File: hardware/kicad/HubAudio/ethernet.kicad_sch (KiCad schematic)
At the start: 29 parts, among them J1 RJ45_Abracon_ARJP11A-MASA-B-A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, U19 LAN8720A, U20 CDCLVC1102PW, X1 ASE-50.000MHZ-LC-T

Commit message: Finalize I2C and SPI control architecture
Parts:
- removed C55: 100nF, Capacitor_SMD:C_0805_2012Metric, symbol Device:C
- removed C56: 1uF, Capacitor_SMD:C_0805_2012Metric, symbol Device:C
- removed C57: 10uF, Capacitor_SMD:C_1206_3216Metric, symbol Device:C
- removed FB2: BLM18BB600SN1, Inductor_SMD:L_0603_1608Metric, symbol Device:FerriteBead
- removed R31, R32: 10K, Resistor_SMD:R_0805_2012Metric, symbol Device:R
- removed RN1: CAY16-49R9F4LF, Resistor_SMD:R_Array_Convex_4x0603, symbol Device:R_Network04_Split
- removed U20: CDCLVC1102PW, Package_SO:TSSOP-8_4.4x3mm_P0.65mm, symbol MIKILAB_CDCLVC1102PW:CDCLVC1102PW
- added R25, R77, R78, R79: 49.9, Resistor_SMD:R_0805_2012Metric, symbol Device:R
- added R80, R81: 33, Resistor_SMD:R_0805_2012Metric, symbol Device:R
- C47, C48, C49, C59, C60, C61: PNM (none) -> GRM21BR71H104KA01L
- C58: PNM (none) -> GRM31CR71E106KA12L
- C62: PNM (none) -> GRM2165C1H471JA01D
- C63: PNM (none) -> GCM21BR71E105KA56L
- R2, R30: value RC0603FR-07330RL -> 330; footprint Inductor_SMD:L_0603_1608Metric -> Resistor_SMD:R_0805_2012Metric; PNM (none) -> RC0805FR-07330RL
- R34: PNM (none) -> FRC0805F1212TS
- R35: PNM (none) -> RC0805FR-074K7L
- R37, R38, R39, R40: PNM (none) -> RC0805FR-0710KL
- U19: PNM (none) -> LAN8720A
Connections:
- net 3V3_ETHERNET: now also R35.1; no longer R35.2
- net ETH_50MHZ_CLOCK: now also R81.2
- net ETH_MDIO: now also R35.2; no longer R35.1
- net ETH_RXD0: now also R37.1
- net ETH_RXD1: now also R38.1
- net ETH_TXD0: no longer R37.1
- net ETH_TXD1: no longer R38.1
- net GND: no longer J1.10 (V-), J1.9 (V+)
- net at U19.20 (TXN): now also R78.1
- net at U19.21 (TXP): now also R77.1
- net at U19.22 (RXN): now also R25.1
- net at U19.23 (RXP): now also R79.1
- net at U19.5 (XTAL1/CLKIN): now also R80.2
- net at J1.1 (TD+): now also R77.2
- net at J1.2 (TD-): now also R78.2
- net at J1.3 (RD+): now also R79.2
- net at J1.6 (RD-): now also R25.2
- net at X1.3 (OUT): now also R80.1, R81.1
- no-connect marks 0 -> 3
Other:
- moved on the sheet: C49, R35, X1

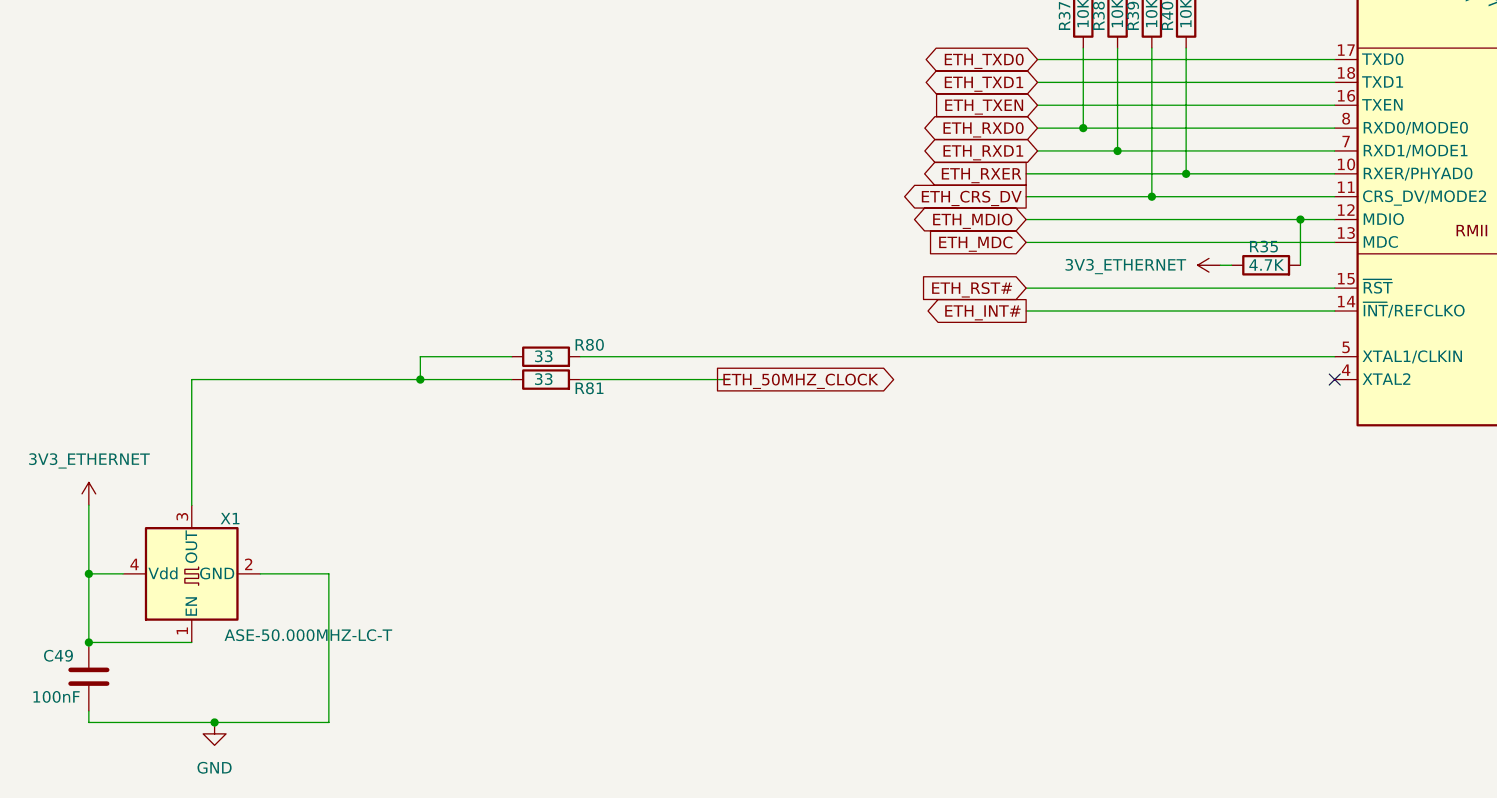
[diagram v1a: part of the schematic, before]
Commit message: Finalize HubAudio hardware architecture and PCB
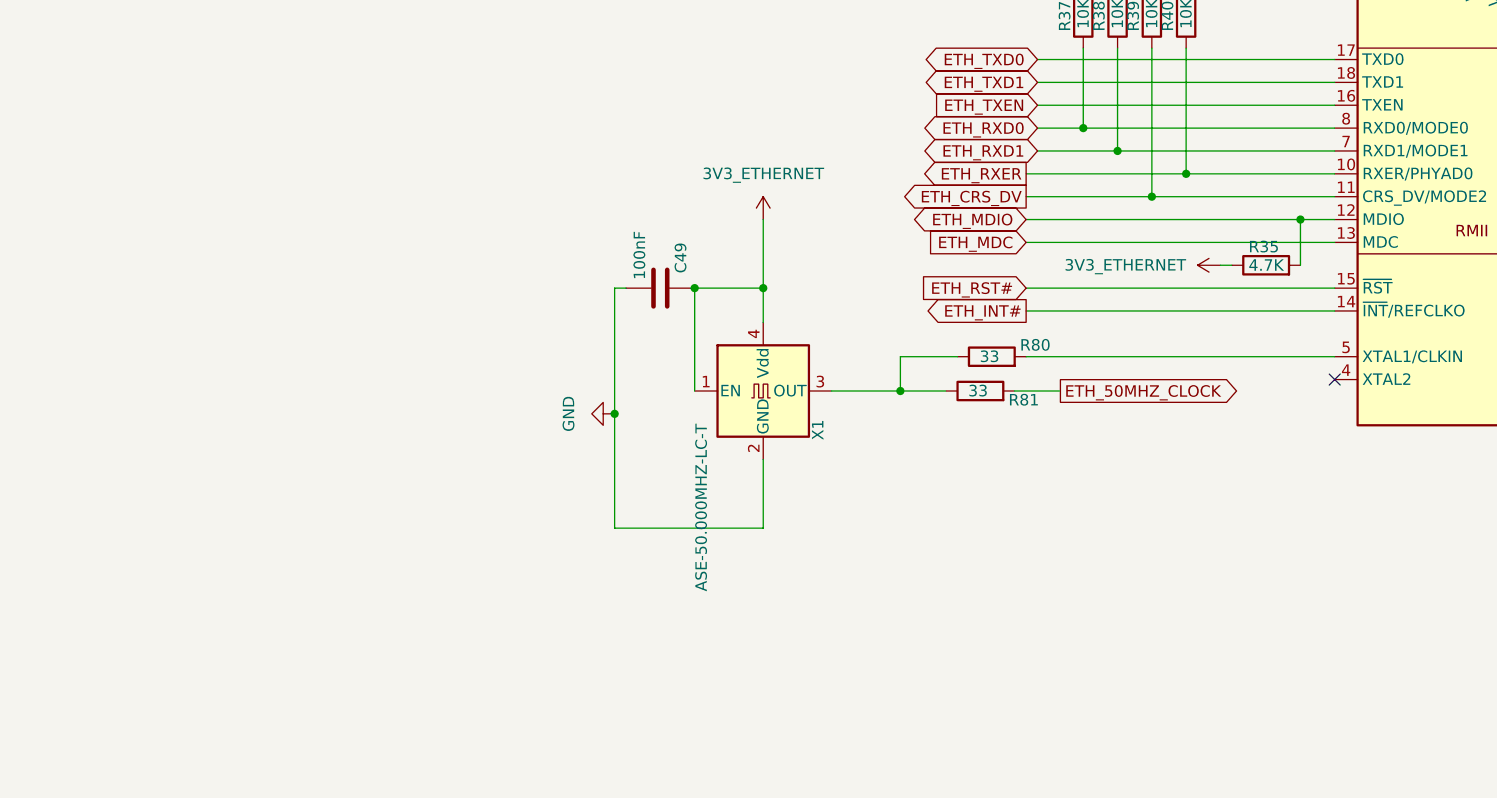
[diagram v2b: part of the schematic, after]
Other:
- moved on the sheet: C49, R80, R81, X1
